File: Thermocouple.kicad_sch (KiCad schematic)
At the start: 3 parts, among them J4 Conn_01x02_Socket, U4 MAX31855KASA

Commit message: done ( v 1.0 - check required )
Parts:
- C5: renamed from C4; footprint (none) -> PCM_JLCPCB:C_0603
- renumbered J4 to J5, U4 to U5
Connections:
- net +3.3V renamed +3V3

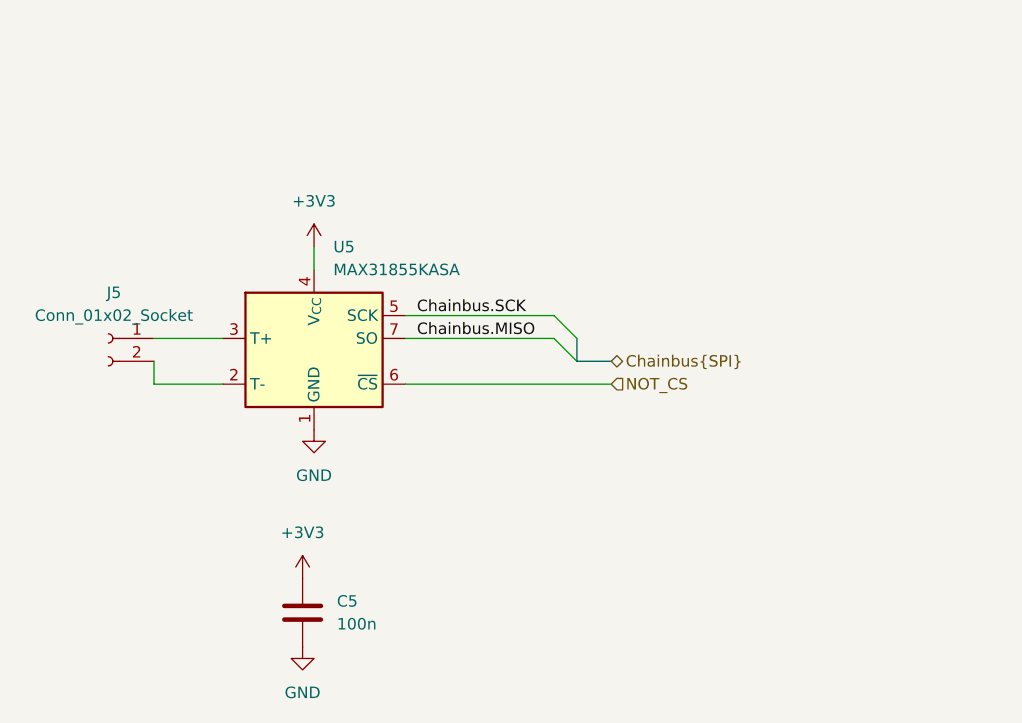
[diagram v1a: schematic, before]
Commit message: fixed selected led polarity
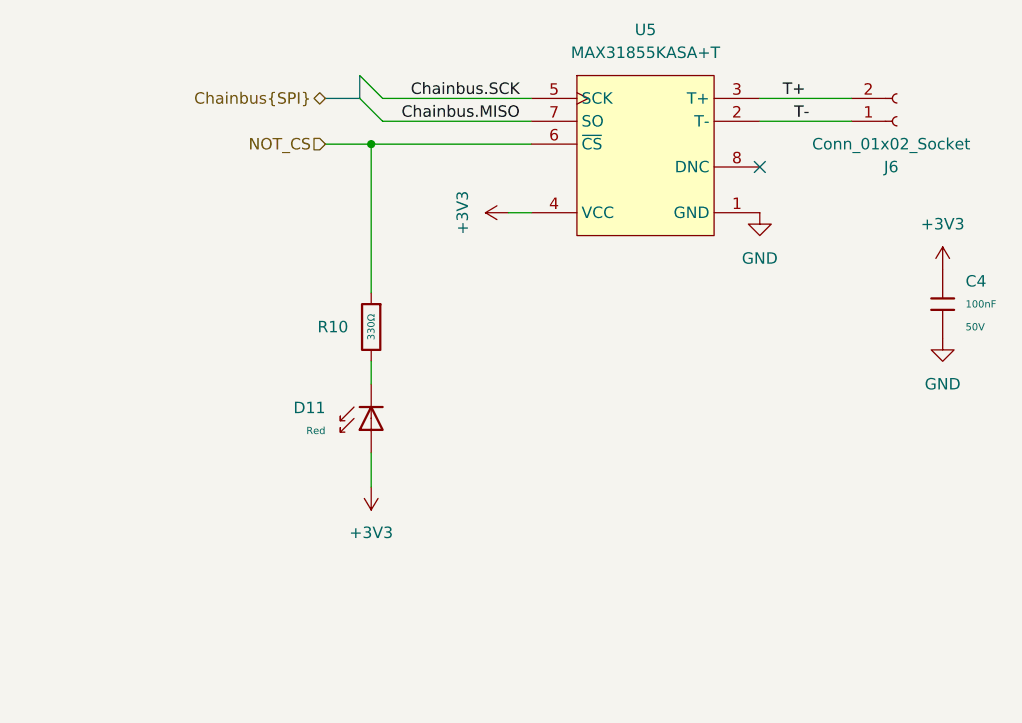
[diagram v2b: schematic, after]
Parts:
- removed C5: 100n, PCM_JLCPCB:C_0603, symbol Device:C
- removed J5: Conn_01x02_Socket, Connector_JST:JST_XH_S2B-XH-A_1x02_P2.50mm_Horizontal, symbol Connector:Conn_01x02_Socket
- removed U5: MAX31855KASA, Package_SO:SOIC-8_3.9x4.9mm_P1.27mm, symbol Sensor_Temperature:MAX31855KASA
- added C4: 100nF, PCM_JLCPCB:C_0603, symbol PCM_JLCPCB-Capacitors:0603,100nF
- added D11: Red, PCM_JLCPCB:D_0603, symbol PCM_JLCPCB-Diodes:LED,0603,Red
- added J6: Conn_01x02_Socket, Connector_JST:JST_XH_S2B-XH-A_1x02_P2.50mm_Horizontal, symbol Connector:Conn_01x02_Socket
- added R10: 330Ω, PCM_JLCPCB:R_0402, symbol PCM_JLCPCB-Resistors:0402,330Ω
- added U5: MAX31855KASA+T, MAX31855KASA:SO-8_L4.9-W3.9-P1.27-LS5.9-BL, symbol MAX31855KASA1:MAX31855KASA+T
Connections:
- net +3V3: now also C4.1, D11.2, U5.4 (VCC)
- net Chainbus.MISO: now also U5.7 (SO)
- net Chainbus.SCK: now also U5.5 (SCK)
- net GND: now also C4.2, U5.1 (GND)
- net NOT_CS: now also R10.1, U5.6 (~{CS})
- new net: D11.1, R10.2
- new net T+: J6.2 (Pin_2), U5.3 (T+)
- new net T-: J6.1 (Pin_1), U5.2 (T-)
- no-connect marks 0 -> 1
